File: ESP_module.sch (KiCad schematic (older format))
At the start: 13 parts, among them SW1 SW_PUSH, SW2 SW_PUSH, U2 APE8865Y5-33-HF-3, U3 ESP-12E

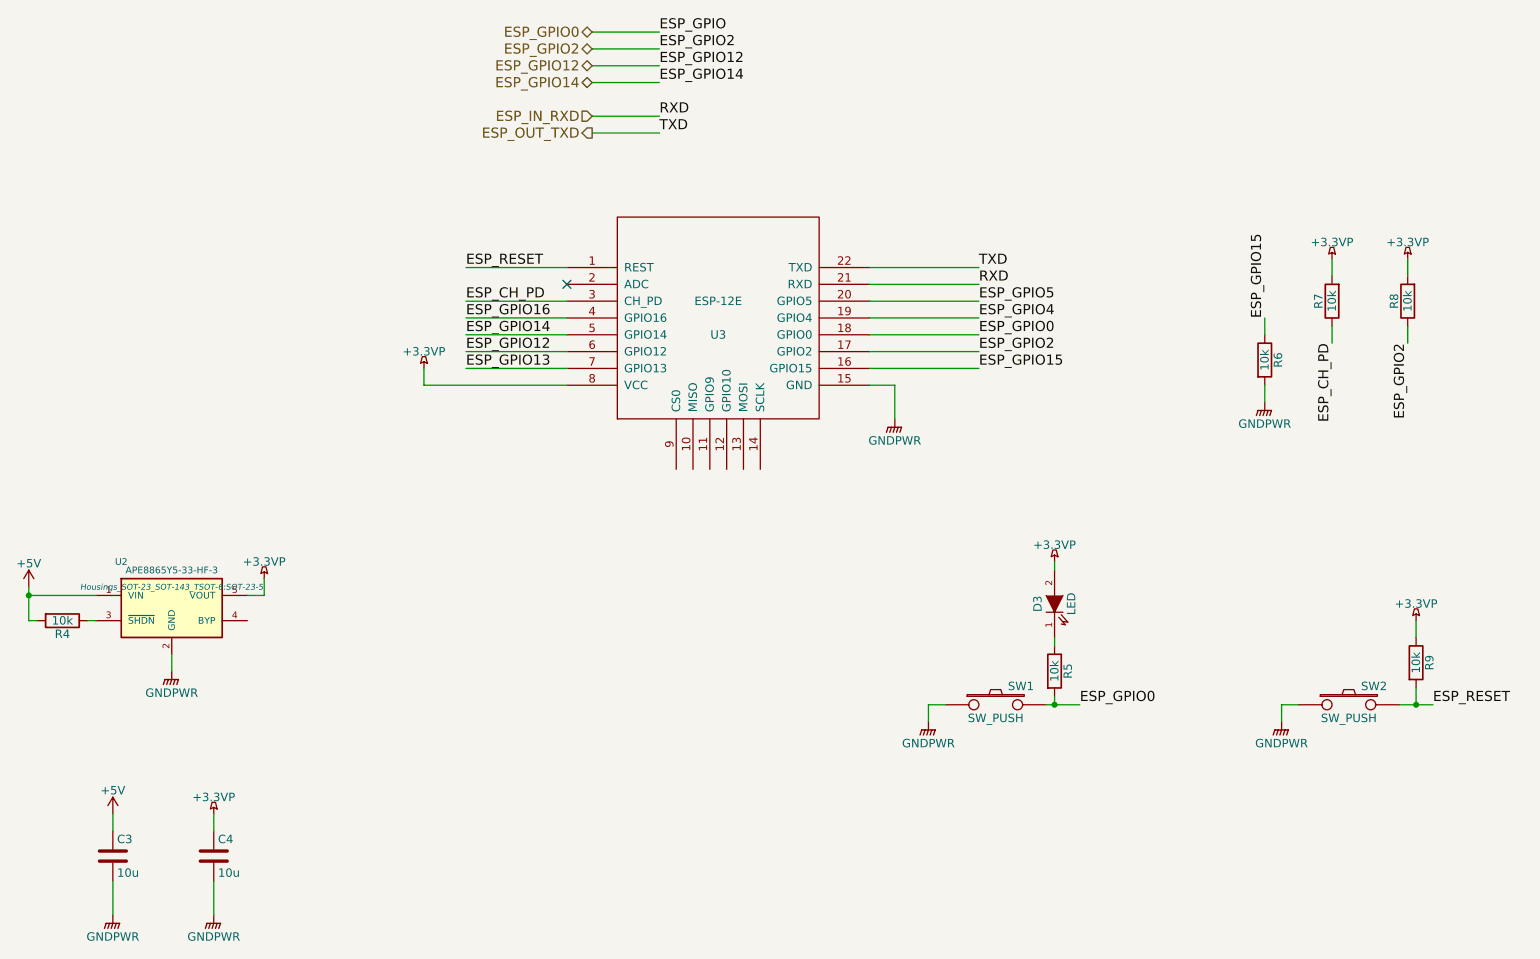
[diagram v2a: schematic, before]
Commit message: Added a USB socket with GND set as a power output to pass DRC, and gave a first stab at a placement. Man that's tight! Components both side required??
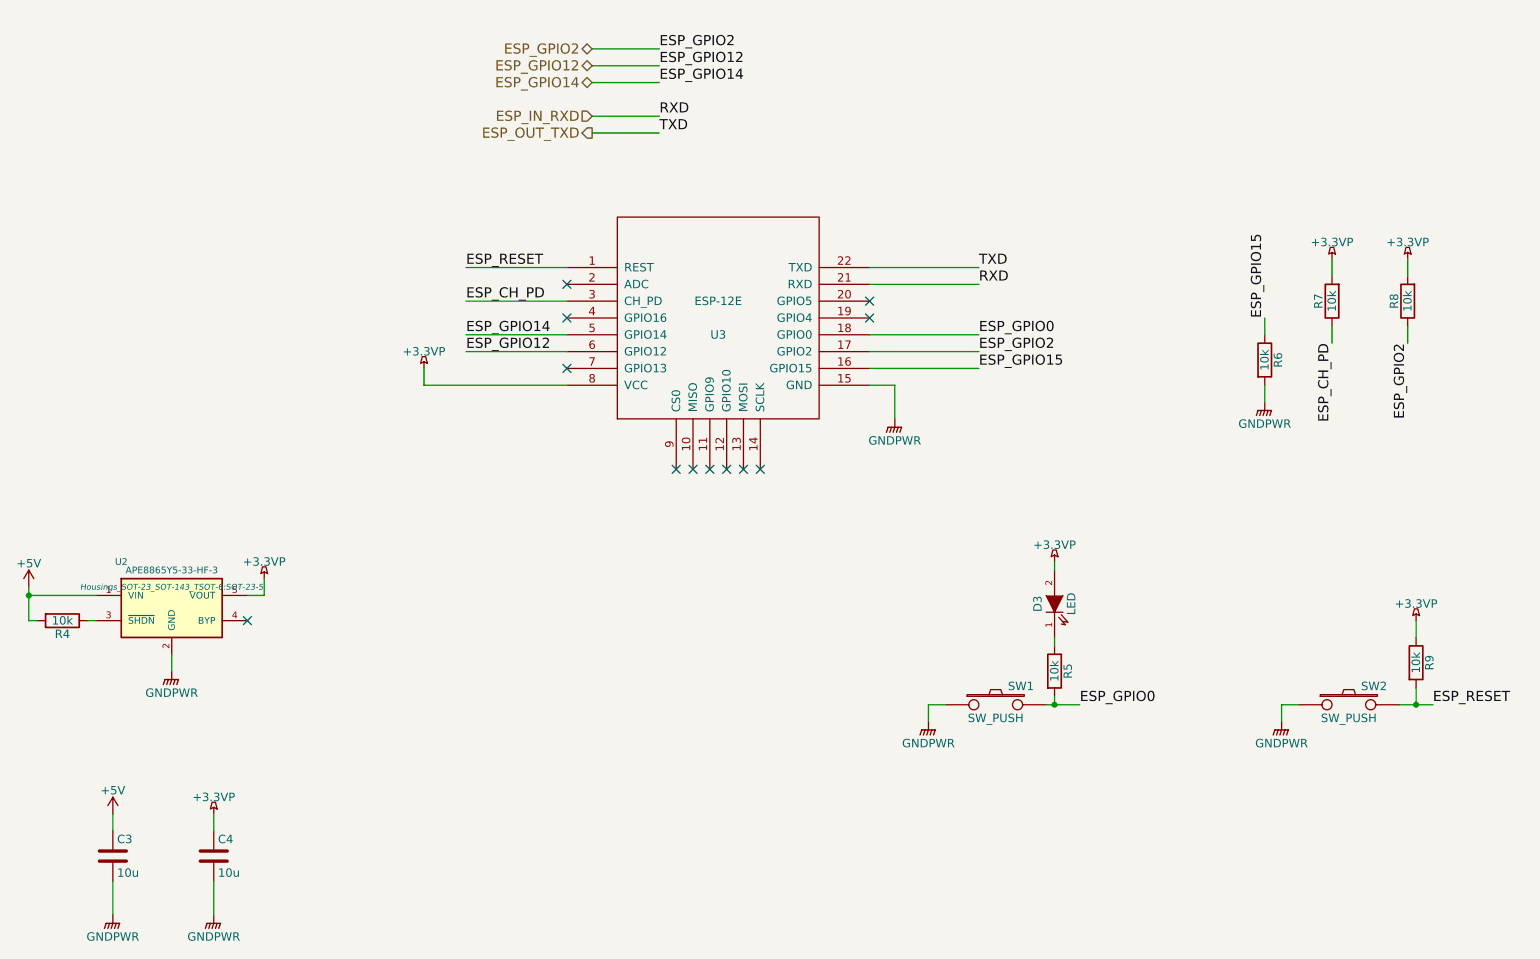
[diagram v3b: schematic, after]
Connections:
- net ESP_GPIO13: no longer names the net of U3.7 (GPIO13)
- net ESP_GPIO16: no longer names the net of U3.4 (GPIO16)
- net ESP_GPIO4: no longer names the net of U3.19 (GPIO4)
- net ESP_GPIO5: no longer names the net of U3.20 (GPIO5)
- no-connect marks 1 -> 12
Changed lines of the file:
@@
 Wire Wire Line
 	3050 6000 3050 6200
-Text HLabel 5300 950  0    60   BiDi ~ 0
-ESP_GPIO0
 Text HLabel 5300 1050 0    60   BiDi ~ 0
 ESP_GPIO2
@@
 Text Label 7600 2450 0    60   ~ 0
 RXD
-Text Label 7600 2550 0    60   ~ 0
-ESP_GPIO5
-Text Label 7600 2650 0    60   ~ 0
-ESP_GPIO4
-Text Label 4550 2650 0    60   ~ 0
-ESP_GPIO16
-Text Label 4550 2750 0    60   ~ 0
-ESP_GPIO14
-Text Label 4550 2850 0    60   ~ 0
-ESP_GPIO12
-Text Label 4550 2950 0    60   ~ 0
-ESP_GPIO13
 Wire Wire Line
 	6950 2350 7600 2350
@@
 	7600 2450 6950 2450
 Wire Wire Line
-	6950 2550 7600 2550
-Wire Wire Line
-	7600 2650 6950 2650
-Wire Wire Line
-	5150 2650 4550 2650
-Wire Wire Line
 	4550 2750 5150 2750
 Wire Wire Line
 	5150 2850 4550 2850
-Wire Wire Line
-	4550 2950 5150 2950
 Text HLabel 5300 1150 0    60   BiDi ~ 0
 ESP_GPIO12
 Text HLabel 5300 1250 0    60   BiDi ~ 0
 ESP_GPIO14
-Text Label 5700 950  0    60   ~ 0
-ESP_GPIO
 Text Label 5700 1050 0    60   ~ 0
 ESP_GPIO2
@@
 Text Label 5700 1550 0    60   ~ 0
 TXD
-Wire Wire Line
-	5300 950  5700 950
 Wire Wire Line
 	5300 1050 5700 1050
@@
 	7100 3050 7100 3250
 NoConn ~ 5150 2450
+NoConn ~ 6300 3550
+NoConn ~ 6200 3550
+NoConn ~ 6100 3550
+NoConn ~ 6000 3550
+NoConn ~ 5900 3550
+NoConn ~ 5800 3550
+NoConn ~ 3250 4450
+Text Label 4550 2850 0    60   ~ 0
+ESP_GPIO12
+Text Label 4550 2750 0    60   ~ 0
+ESP_GPIO14
+NoConn ~ 6950 2550
+NoConn ~ 6950 2650
+NoConn ~ 5150 2950
+NoConn ~ 5150 2650
 $EndSCHEMATC

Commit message: Dodgy layout added, etc
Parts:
- SW1, SW2: footprint Buttons_Switches_SMD:SW_SPST_EVQP2 -> EVQP2:SW_SPST_EVQP2
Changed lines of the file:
@@
 EESchema Schematic File Version 2
+LIBS:weatherstation-rescue
 LIBS:power
 LIBS:device
@@
 F 0 "SW2" H 9950 5060 50  0000 C CNN
 F 1 "SW_PUSH" H 9800 4870 50  0000 C CNN
-F 2 "Buttons_Switches_SMD:SW_SPST_EVQP2" H 9800 4950 60  0001 C CNN
+F 2 "EVQP2:SW_SPST_EVQP2" H 9800 4950 60  0001 C CNN
 F 3 "" H 9800 4950 60  0000 C CNN
 	1    9800 4950
@@
 F 0 "SW1" H 7850 5060 50  0000 C CNN
 F 1 "SW_PUSH" H 7700 4870 50  0000 C CNN
-F 2 "Buttons_Switches_SMD:SW_SPST_EVQP2" H 7700 4950 60  0001 C CNN
+F 2 "EVQP2:SW_SPST_EVQP2" H 7700 4950 60  0001 C CNN
 F 3 "" H 7700 4950 60  0000 C CNN
 	1    7700 4950

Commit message: Added some RS part numbers for switches and usb
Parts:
- SW1, SW2: RS_Part (none) -> http://uk.rs-online.com/web/p/tactile-switches/7561789/
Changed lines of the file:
@@
 EESchema Schematic File Version 2
-LIBS:weatherstation-rescue
 LIBS:power
 LIBS:device
@@
 F 2 "EVQP2:SW_SPST_EVQP2" H 9800 4950 60  0001 C CNN
 F 3 "" H 9800 4950 60  0000 C CNN
+F 4 "http://uk.rs-online.com/web/p/tactile-switches/7561789/" H 9800 4950 60  0001 C CNN "RS_Part"
 	1    9800 4950
 	1    0    0    -1
@@
 F 2 "EVQP2:SW_SPST_EVQP2" H 7700 4950 60  0001 C CNN
 F 3 "" H 7700 4950 60  0000 C CNN
+F 4 "http://uk.rs-online.com/web/p/tactile-switches/7561789/" H 7700 4950 60  0001 C CNN "RS_Part"
 	1    7700 4950
 	1    0    0    -1
